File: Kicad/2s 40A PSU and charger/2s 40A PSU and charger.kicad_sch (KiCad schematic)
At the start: 5 parts

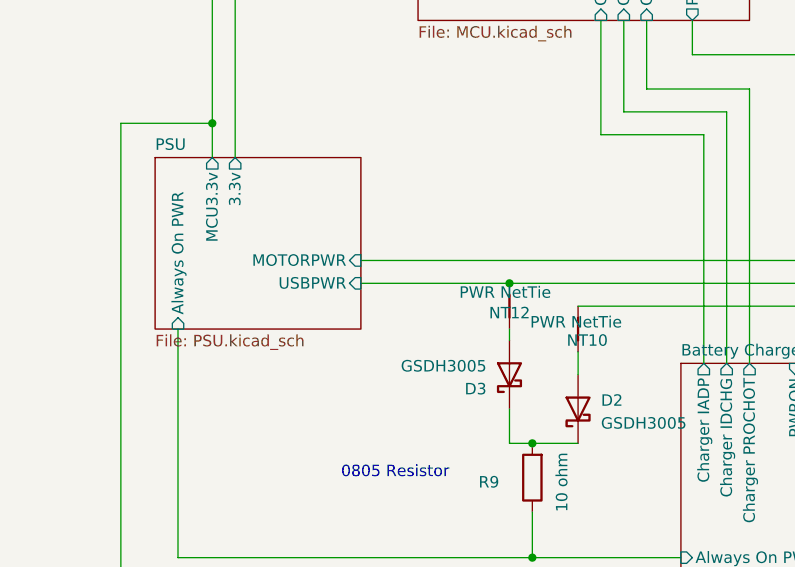
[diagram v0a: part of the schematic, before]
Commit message: Combined separate ground planes
I now have one solid ground plane. There really was no point in having separate ground planes EXCEPT for keeping the high current return path away from the MCU and sense lines. I have added a keepout zone on the top half, to split to keep the high current return from going into the MCU section, but that is it.
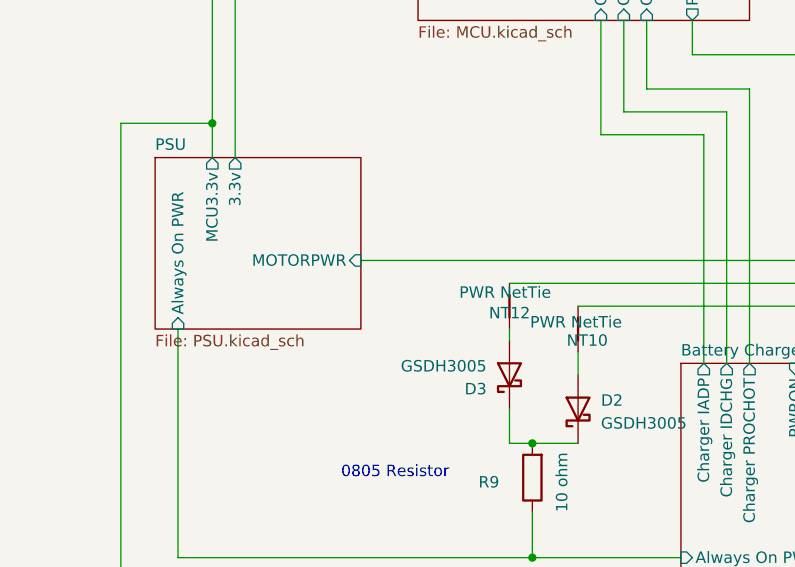
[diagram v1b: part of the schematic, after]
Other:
- sheet PSU ports: added none; removed USBPWR
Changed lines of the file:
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@@
-	)
-	(junction
-		(at 107.95 116.84)
-		(diameter 0)
-		(color 0 0 0 0)
 	)
 	(junction
@@
 		(pts
 			(xy 107.95 134.62) (xy 110.49 134.62)
-		)
-		(stroke
-			(width 0)
-			(type default)
-		)
-	)
-	(wire
-		(pts
-			(xy 91.44 116.84) (xy 107.95 116.84)
 		)
 		(stroke
@@
 			(effects
 				(font
-					(size 1.27 1.27)
-				)
-				(justify right)
-			)
-		)
-		(pin "USBPWR" input
-			(at 91.44 116.84 0)
-			(effects
-				(font

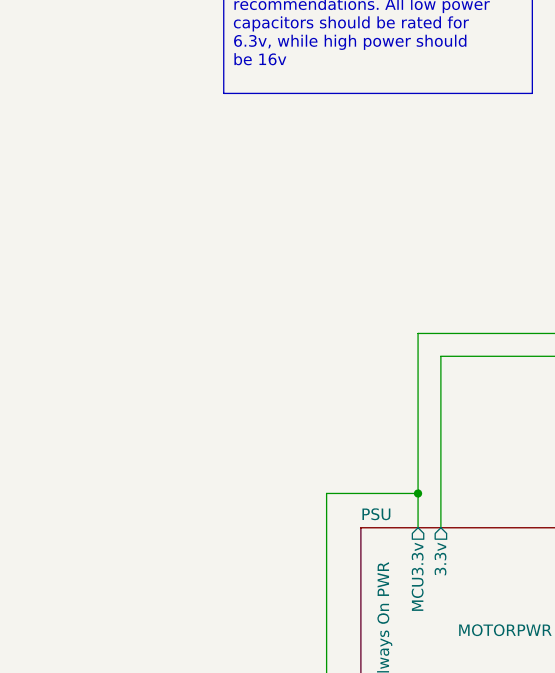
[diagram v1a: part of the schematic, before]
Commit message: Fixed incorrect mosfet pin assignments
This was an issue from the last test board I designed that I didn't catch. The mosfets have different pin assignments for drain, gate, and source, and I had messed those up in the schematic by choosing the wrong symbol. This should be fixed now
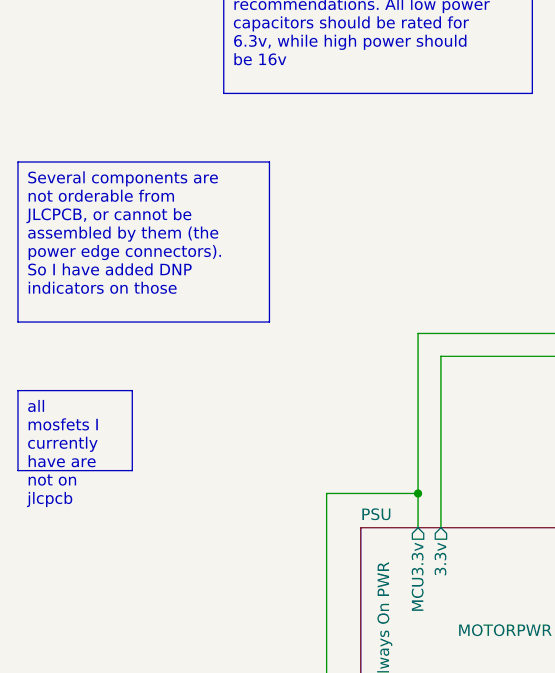
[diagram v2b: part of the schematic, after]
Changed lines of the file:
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@@
+		)
+	)
+	(text_box "Several components are not orderable from JLCPCB, or cannot be assembled by them (the power edge connectors). So I have added DNP indicators on those"
+		(exclude_from_sim no)
+		(at 30.48 62.23 0)
+		(size 27.94 17.78)
+		(stroke
+			(width 0)
+			(type default)
+		)
+		(fill
+			(type none)
+		)
+		(effects
+			(font
+				(size 1.27 1.27)
+			)
+			(justify left top)
+		)
+	)
+	(text_box "all mosfets I currently have are not on jlcpcb"
+		(exclude_from_sim no)
+		(at 30.48 87.63 0)
+		(size 12.7 8.89)
+		(stroke
+			(width 0)
+			(type default)
+		)
+		(fill
+			(type none)
+		)
+		(effects
+			(font
+				(size 1.27 1.27)
+			)
+			(justify left top)
 		)
 	)

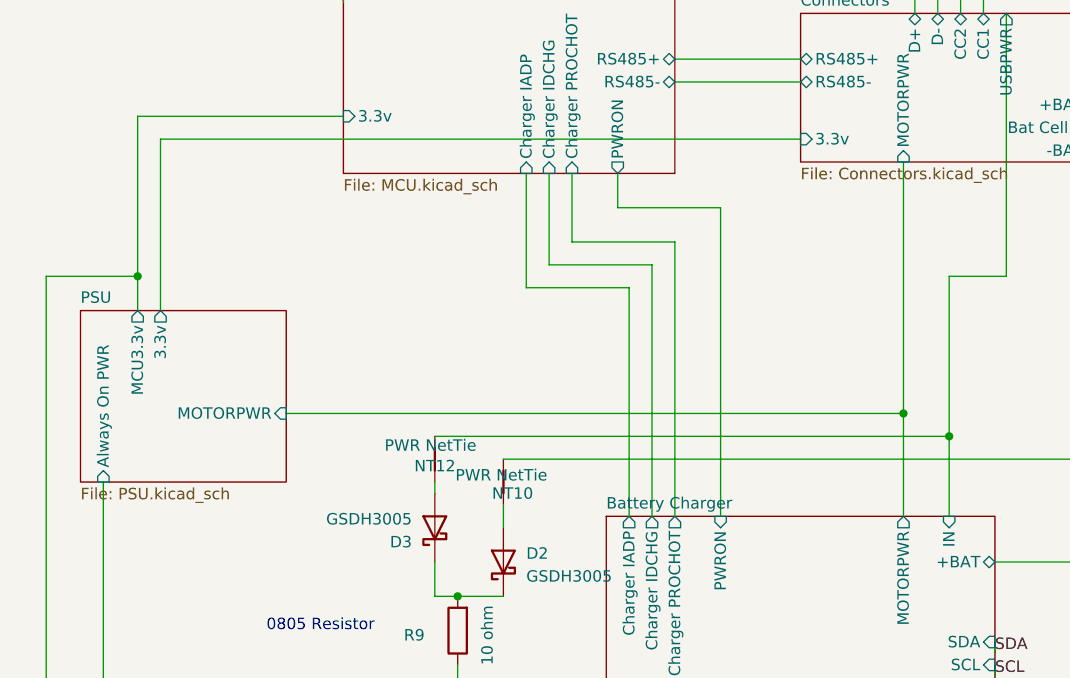
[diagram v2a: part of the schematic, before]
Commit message: Final tweaks, capacitor placement and GND keepouts
I tried my best to isolate signal grounds from the power paths. I also added a bunch of ground keepouts to help isolate.
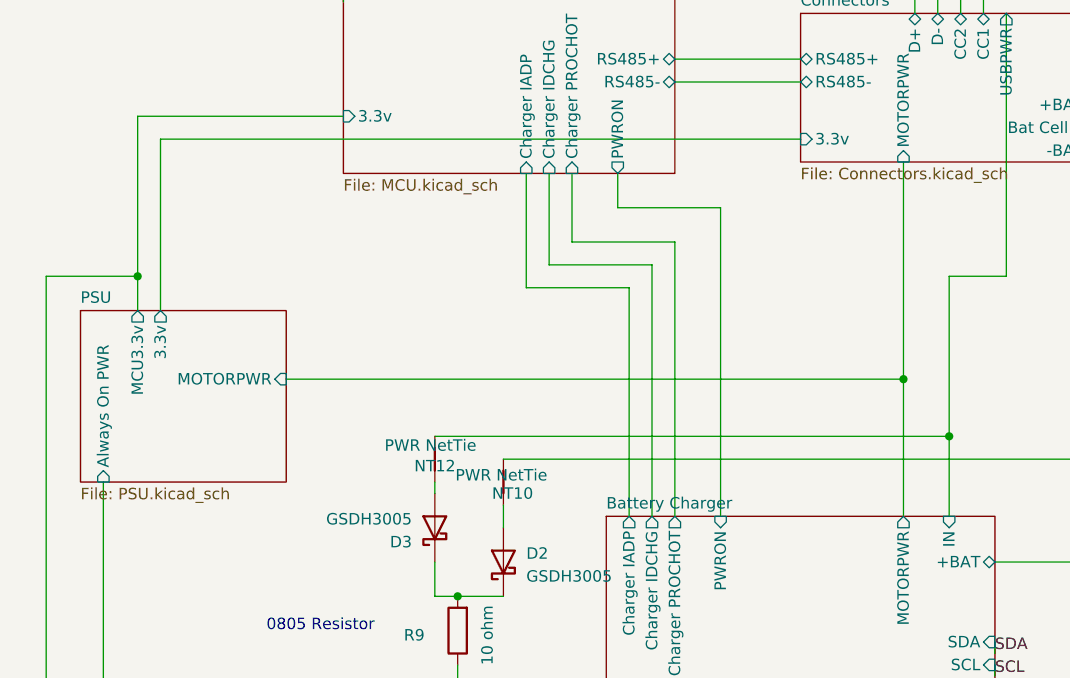
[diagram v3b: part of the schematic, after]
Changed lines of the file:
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@@
 	(title_block
 		(title "CACKLE 2s 40A PSU & Charger")
-		(date "2024-12-01")
+		(date "2024-12-23")
 		(rev "V1")
 		(comment 1 "Author: Asher Edwards")
@@
 	)
 	(junction
-		(at 160.02 114.3)
+		(at 189.23 119.38)
 		(diameter 0)
 		(color 0 0 0 0)
 	)
 	(junction
-		(at 189.23 119.38)
+		(at 160.02 110.49)
 		(diameter 0)
 		(color 0 0 0 0)
@@
 	(wire
 		(pts
-			(xy 91.44 114.3) (xy 160.02 114.3)
+			(xy 91.44 110.49) (xy 160.02 110.49)
 		)
 		(stroke
@@
 	(wire
 		(pts
-			(xy 160.02 86.36) (xy 160.02 114.3)
+			(xy 160.02 86.36) (xy 160.02 110.49)
 		)
 		(stroke
@@
 	(wire
 		(pts
-			(xy 160.02 114.3) (xy 160.02 125.73)
-		)
-		(stroke
-			(width 0)
-			(type default)
-		)
-	)
-	(wire
-		(pts
 			(xy 189.23 130.81) (xy 170.18 130.81)
 		)
@@
 		(pts
 			(xy 171.45 99.06) (xy 171.45 69.85)
+		)
+		(stroke
+			(width 0)
+			(type default)
+		)
+	)
+	(wire
+		(pts
+			(xy 160.02 110.49) (xy 160.02 125.73)
 		)
 		(stroke
@@
 		)
 		(pin "MOTORPWR" input
-			(at 91.44 114.3 0)
-			(effects
-				(font
+			(at 91.44 110.49 0)
+			(effects
+				(font

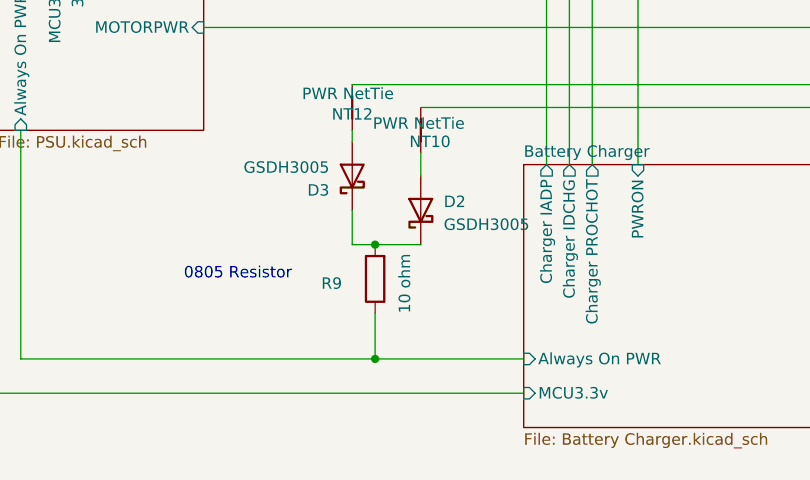
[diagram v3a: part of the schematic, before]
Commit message: Added LCSC part numbers, DNP attr, and exported Gerbers
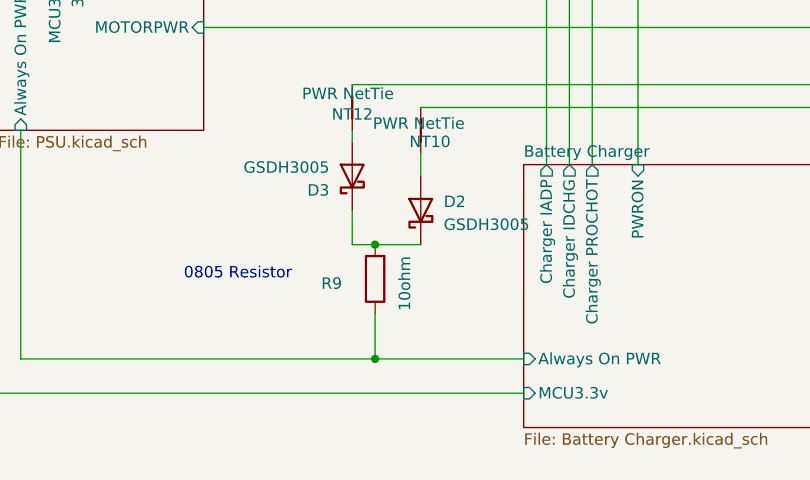
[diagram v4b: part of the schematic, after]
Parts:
- D2, D3: LCSC (none) -> C2837790
- R9: value 10 ohm -> 10ohm; LCSC (none) -> C17415
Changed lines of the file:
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@@
 			)
 		)
-		(property "Value" "10 ohm"
+		(property "Value" "10ohm"
 			(at 113.792 138.938 90)
 			(effects
@@
 		(property "Description" "Resistor"
 			(at 110.49 138.43 0)
+			(effects
+				(font
+					(size 1.27 1.27)
+				)
+				(hide yes)
+			)
+		)
+		(property "LCSC" "C17415"
+			(at 105.664 138.938 0)
 			(effects
 				(font
@@
 			)
 		)
+		(property "LCSC" "C2837790"
+			(at 105.41 128.5876 0)
+			(effects
+				(font
+					(size 1.27 1.27)
+				)
+				(hide yes)
+			)
+		)
 		(pin "2"
 		)
@@
 			(effects
 				(font
+					(size 1.27 1.27)
+				)
+				(hide yes)
+			)
+		)
+		(property "LCSC" "C2837790"
+			(at 118.11 129.8574 0)
+			(effects
+				(font
